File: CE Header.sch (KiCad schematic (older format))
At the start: 1 part

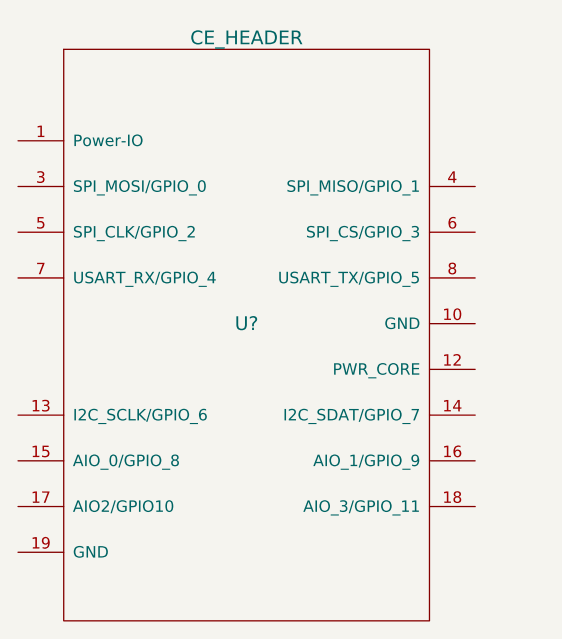
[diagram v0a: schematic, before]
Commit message: Added new directory for example project
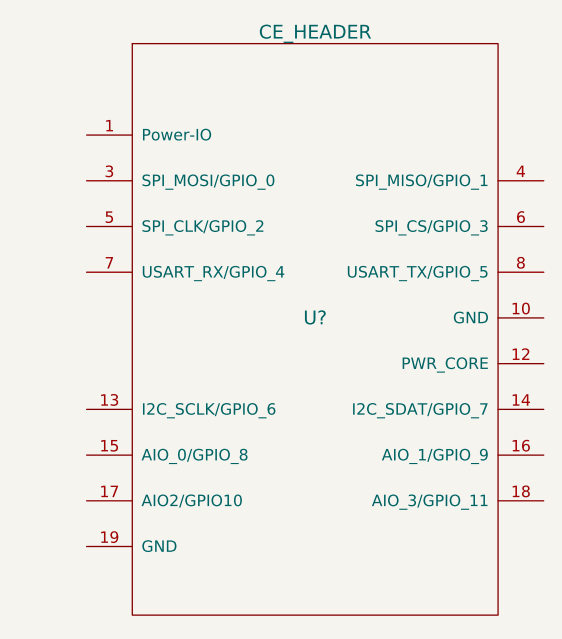
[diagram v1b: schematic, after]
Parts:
- removed U?: CE_HEADER, symbol CE_HEADER
- added U?: CE_HEADER, symbol CE_HEADER
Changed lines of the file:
@@
 EESchema Schematic File Version 2
+LIBS:CE Header-rescue
 LIBS:power
 LIBS:device
@@
 LIBS:valves
 LIBS:ce_header
+LIBS:CE Header-cache
 EELAYER 25 0
 EELAYER END
@@
 $Comp
 L CE_HEADER U?
-U 1 1 58A1EF73
-P 3350 3275
-F 0 "U?" H 3350 3275 60  0000 C CNN
-F 1 "CE_HEADER" H 3350 4525 60  0000 C CNN
-F 2 "" H 3350 3275 60  0001 C CNN
-F 3 "" H 3350 3275 60  0001 C CNN
-	1    3350 3275
+U 1 1 58A723CD
+P 3650 3250
+F 0 "U?" H 3650 3250 60  0000 C CNN
+F 1 "CE_HEADER" H 3650 4500 60  0000 C CNN
+F 2 "" H 3650 3250 60  0001 C CNN
+F 3 "" H 3650 3250 60  0001 C CNN
+	1    3650 3250
 	1    0    0    -1
 $EndComp
